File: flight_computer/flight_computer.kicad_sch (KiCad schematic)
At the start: 2 parts, among them U2 STM8S007C8T6

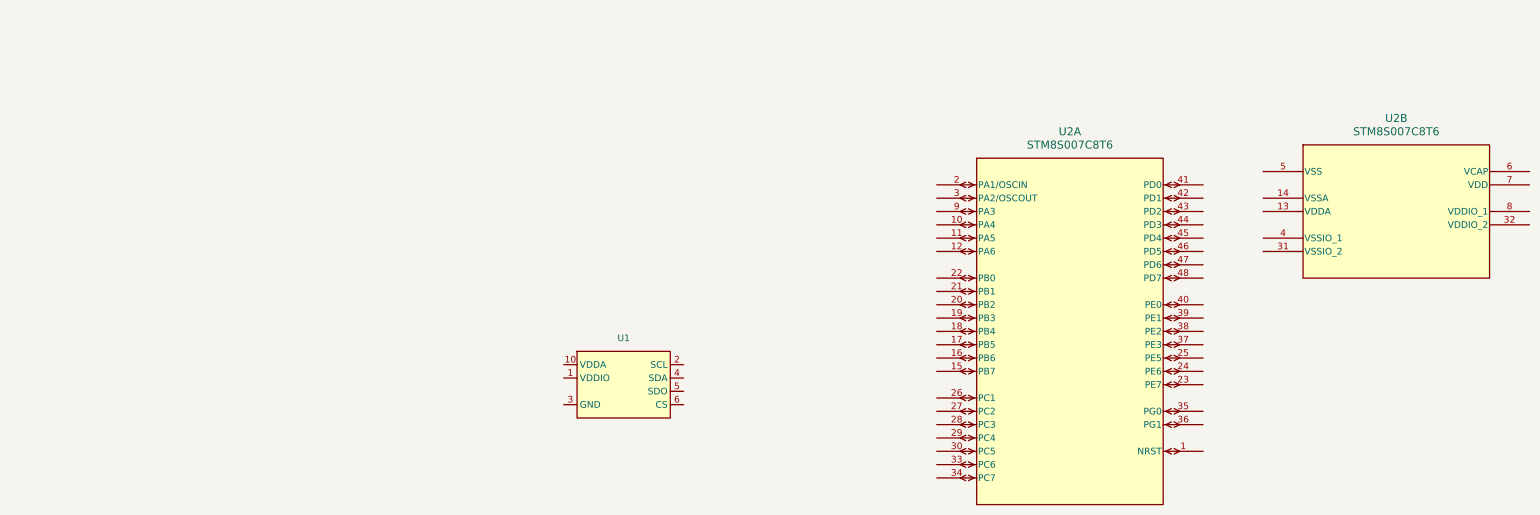
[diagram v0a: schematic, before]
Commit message: Finished power input design
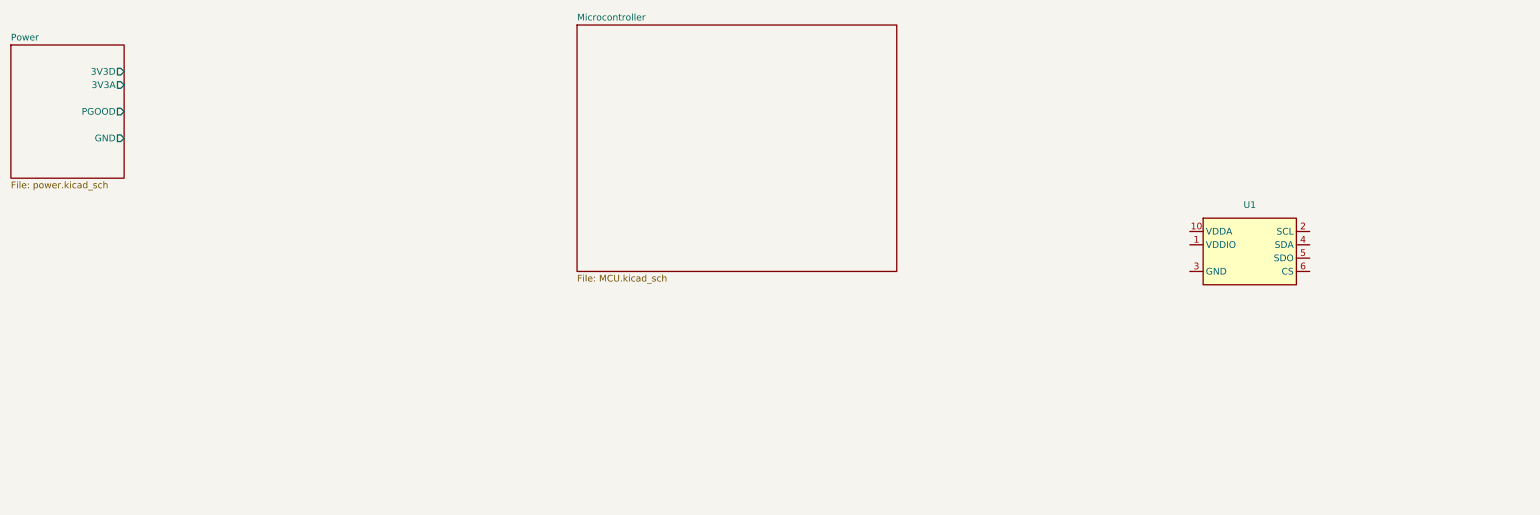
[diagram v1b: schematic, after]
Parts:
- removed U2: STM8S007C8T6, Package_QFP:LQFP-48_7x7mm_P0.5mm, symbol my_library:STM8S007C8T6
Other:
- added sheet Microcontroller (MCU.kicad_sch)
- added sheet Power (power.kicad_sch)
- moved on the sheet: U1
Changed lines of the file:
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@@
 (kicad_sch (version 20230121) (generator eeschema)
   (paper "A3")
-  (symbol (lib_id "my_library:STM8S007C8T6") (at 273.05 113.03 0) (unit 1)
+  (symbol (lib_id "my_library:SPL07-003") (at 307.34 97.79 0) (unit 1)
     (in_bom yes) (on_board yes) (dnp no) (fields_autoplaced)
-    (property "Reference" "U2" (at 273.05 74.93 0)
-      (effects (font (size 1.524 1.524)))
-    )
-    (property "Value" "STM8S007C8T6" (at 273.05 77.47 0)
-      (effects (font (size 1.524 1.524)))
-    )
-    (property "Footprint" "Package_QFP:LQFP-48_7x7mm_P0.5mm" (at 247.65 85.09 0)
-      (effects (font (size 1.27 1.27) italic) hide)
-    )
-    (property "Datasheet" "https://www.st.com/content/ccc/resource/technical/document/datasheet/03/af/ba/15/7c/fe/4c/91/DM00037365.pdf/files/DM00037365.pdf/jcr:content/translations/en.DM00037365.pdf" (at 247.65 85.09 0)
-      (effects (font (size 1.27 1.27) italic) hide)
-    )
-    (pin "1")
-    (pin "10")
-    (pin "11")
-    (pin "12")
-    (pin "15")
-    (pin "16")
-    (pin "17")
-    (pin "18")
-    (pin "19")
-    (pin "2")
-    (pin "20")
-    (pin "21")
-    (pin "22")
-    (pin "23")
-    (pin "24")
-    (pin "25")
-    (pin "26")
-    (pin "27")
-    (pin "28")
-    (pin "29")
-    (pin "3")
-    (pin "30")
-    (pin "33")
-    (pin "34")
-    (pin "35")
-    (pin "36")
-    (pin "37")
-    (pin "38")
-    (pin "39")
-    (pin "40")
-    (pin "41")
-    (pin "42")
-    (pin "43")
-    (pin "44")
-    (pin "45")
-    (pin "46")
-    (pin "47")
-    (pin "48")
-    (pin "9")
-    (pin "13")
-    (pin "14")
-    (pin "31")
-    (pin "32")
-    (pin "4")
-    (pin "5")
-    (pin "6")
-    (pin "7")
-    (pin "8")
-    (instances
-      (project "flight_computer"
-        (path "/89a81c02-14e9-456f-a334-ff69a24bd093"
-          (reference "U2") (unit 1)
-        )
-      )
-    )
-  )
-  (symbol (lib_id "my_library:STM8S007C8T6") (at 335.28 90.17 0) (unit 2)
-    (in_bom yes) (on_board yes) (dnp no) (fields_autoplaced)
-    (property "Reference" "U2" (at 335.28 72.39 0)
-      (effects (font (size 1.524 1.524)))
-    )
-    (property "Value" "STM8S007C8T6" (at 335.28 74.93 0)
-      (effects (font (size 1.524 1.524)))
-    )
-    (property "Footprint" "Package_QFP:LQFP-48_7x7mm_P0.5mm" (at 309.88 62.23 0)
-      (effects (font (size 1.27 1.27) italic) hide)
-    )
-    (property "Datasheet" "https://www.st.com/content/ccc/resource/technical/document/datasheet/03/af/ba/15/7c/fe/4c/91/DM00037365.pdf/files/DM00037365.pdf/jcr:content/translations/en.DM00037365.pdf" (at 309.88 62.23 0)
-      (effects (font (size 1.27 1.27) italic) hide)
-    )
-    (pin "1")
-    (pin "10")
-    (pin "11")
-    (pin "12")
-    (pin "15")
-    (pin "16")
-    (pin "17")
-    (pin "18")
-    (pin "19")
-    (pin "2")
-    (pin "20")
-    (pin "21")
-    (pin "22")
-    (pin "23")
-    (pin "24")
-    (pin "25")
-    (pin "26")
-    (pin "27")
-    (pin "28")
-    (pin "29")
-    (pin "3")
-    (pin "30")
-    (pin "33")
-    (pin "34")
-    (pin "35")
-    (pin "36")
-    (pin "37")
-    (pin "38")
-    (pin "39")
-    (pin "40")
-    (pin "41")
-    (pin "42")
-    (pin "43")
-    (pin "44")
-    (pin "45")
-    (pin "46")
-    (pin "47")
-    (pin "48")
-    (pin "9")
-    (pin "13")
-    (pin "14")
-    (pin "31")
-    (pin "32")
-    (pin "4")
-    (pin "5")
-    (pin "6")
-    (pin "7")
-    (pin "8")
-    (instances
-      (project "flight_computer"
-        (path "/89a81c02-14e9-456f-a334-ff69a24bd093"
-          (reference "U2") (unit 2)
-        )
-      )
-    )
-  )
-  (symbol (lib_id "my_library:SPL07-003") (at 187.96 123.19 0) (unit 1)
-    (in_bom yes) (on_board yes) (dnp no) (fields_autoplaced)
-    (property "Reference" "U1" (at 187.96 114.3 0)
+    (property "Reference" "U1" (at 307.34 88.9 0)
       (effects (font (size 1.27 1.27)))
     )
-    (property "Value" "~" (at 187.96 127 0)
+    (property "Value" "~" (at 307.34 101.6 0)
       (effects (font (size 1.27 1.27)))
     )
-    (property "Footprint" "Package_LGA:ST_HLGA-10_2x2mm_P0.5mm_LayoutBorder3x2y" (at 187.96 127 0)
+    (property "Footprint" "Package_LGA:ST_HLGA-10_2x2mm_P0.5mm_LayoutBorder3x2y" (at 307.34 101.6 0)
       (effects (font (size 1.27 1.27)) hide)
     )
-    (property "Datasheet" "https://mm.digikey.com/Volume0/opasdata/d220001/medias/docus/4843/SPL07-003.pdf" (at 187.96 127 0)
+    (property "Datasheet" "https://mm.digikey.com/Volume0/opasdata/d220001/medias/docus/4843/SPL07-003.pdf" (at 307.34 101.6 0)
       (effects (font (size 1.27 1.27)) hide)
     )
-    (property "Manufacturer PN" "" (at 187.96 123.19 0)
+    (property "Manufacturer PN" "" (at 307.34 97.79 0)
       (effects (font (size 1.27 1.27)) hide)
     )
-    (property "Supplier PN" "" (at 187.96 123.19 0)
+    (property "Supplier PN" "" (at 307.34 97.79 0)
       (effects (font (size 1.27 1.27)) hide)
     )
-    (property "Supplier" "" (at 187.96 123.19 0)
+    (property "Supplier" "" (at 307.34 97.79 0)
       (effects (font (size 1.27 1.27)) hide)
     )
@@
       )
     )
+  )
+  (sheet (at 179.07 54.61) (size 60.96 46.99) (fields_autoplaced)
+    (stroke (width 0.1524) (type solid))
+    (fill (color 0 0 0 0.0000))
+    (property "Sheetname" "Microcontroller" (at 179.07 53.8984 0)
+      (effects (font (size 1.27 1.27)) (justify left bottom))
+    )
+    (property "Sheetfile" "MCU.kicad_sch" (at 179.07 102.1846 0)
+      (effects (font (size 1.27 1.27)) (justify left top))
+    )
+    (instances
+      (project "flight_computer"
+        (path "/89a81c02-14e9-456f-a334-ff69a24bd093" (page "2"))
+      )
+    )
+  )
+  (sheet (at 71.12 58.42) (size 21.59 25.4) (fields_autoplaced)
+    (stroke (width 0.1524) (type solid))
+    (fill (color 0 0 0 0.0000))
+    (property "Sheetname" "Power" (at 71.12 57.7084 0)
+      (effects (font (size 1.27 1.27)) (justify left bottom))
+    )
+    (property "Sheetfile" "power.kicad_sch" (at 71.12 84.4046 0)
+      (effects (font (size 1.27 1.27)) (justify left top))
+    )
+    (pin "PGOOD" output (at 92.71 71.12 0)
+      (effects (font (size 1.27 1.27)) (justify right))
+    )
+    (pin "GND" output (at 92.71 76.2 0)
+      (effects (font (size 1.27 1.27)) (justify right))
+    )
+    (pin "3V3D" output (at 92.71 63.5 0)
+      (effects (font (size 1.27 1.27)) (justify right))
+    )
+    (pin "3V3A" output (at 92.71 66.04 0)
+      (effects (font (size 1.27 1.27)) (justify right))
+    )
+    (instances
+      (project "flight_computer"
+        (path "/89a81c02-14e9-456f-a334-ff69a24bd093" (page "3"))
+      )
+    )

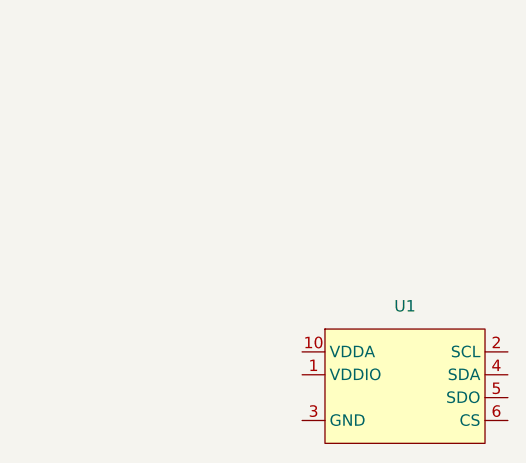
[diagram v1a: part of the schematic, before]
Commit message: Buzzer, LEDs, added actual components for current sensing and others I had missed
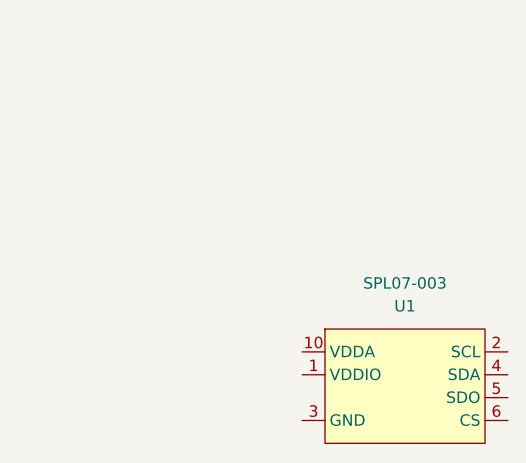
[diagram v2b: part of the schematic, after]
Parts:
- U1: value ~ -> SPL07-003; Manufacturer PN (none) -> SPL07-003; Supplier (none) -> Digikey; Supplier PN (none) -> 4719-SPL07-003CT-ND
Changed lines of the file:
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@@
   (paper "A3")
   (symbol (lib_id "my_library:SPL07-003") (at 307.34 97.79 0) (unit 1)
-    (in_bom yes) (on_board yes) (dnp no) (fields_autoplaced)
+    (in_bom yes) (on_board yes) (dnp no)
     (property "Reference" "U1" (at 307.34 88.9 0)
       (effects (font (size 1.27 1.27)))
     )
-    (property "Value" "~" (at 307.34 101.6 0)
+    (property "Value" "SPL07-003" (at 307.34 86.36 0)
       (effects (font (size 1.27 1.27)))
     )
@@
       (effects (font (size 1.27 1.27)) hide)
     )
-    (property "Manufacturer PN" "" (at 307.34 97.79 0)
+    (property "Manufacturer PN" "SPL07-003" (at 307.34 97.79 0)
       (effects (font (size 1.27 1.27)) hide)
     )
-    (property "Supplier PN" "" (at 307.34 97.79 0)
+    (property "Supplier PN" "4719-SPL07-003CT-ND" (at 307.34 97.79 0)
       (effects (font (size 1.27 1.27)) hide)
     )
-    (property "Supplier" "" (at 307.34 97.79 0)
+    (property "Supplier" "Digikey" (at 307.34 97.79 0)
       (effects (font (size 1.27 1.27)) hide)
     )

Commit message: PRessure sensor circuit
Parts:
- removed U1: SPL07-003, Package_LGA:ST_HLGA-10_2x2mm_P0.5mm_LayoutBorder3x2y, symbol my_library:SPL07-003
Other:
- added sheet Sensors (sensors.kicad_sch)
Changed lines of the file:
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@@
 (kicad_sch (version 20230121) (generator eeschema)
   (paper "A3")
-  (symbol (lib_id "my_library:SPL07-003") (at 307.34 97.79 0) (unit 1)
-    (in_bom yes) (on_board yes) (dnp no)
-    (property "Reference" "U1" (at 307.34 88.9 0)
-      (effects (font (size 1.27 1.27)))
-    )
-    (property "Value" "SPL07-003" (at 307.34 86.36 0)
-      (effects (font (size 1.27 1.27)))
-    )
-    (property "Footprint" "Package_LGA:ST_HLGA-10_2x2mm_P0.5mm_LayoutBorder3x2y" (at 307.34 101.6 0)
-      (effects (font (size 1.27 1.27)) hide)
-    )
-    (property "Datasheet" "https://mm.digikey.com/Volume0/opasdata/d220001/medias/docus/4843/SPL07-003.pdf" (at 307.34 101.6 0)
-      (effects (font (size 1.27 1.27)) hide)
-    )
-    (property "Manufacturer PN" "SPL07-003" (at 307.34 97.79 0)
-      (effects (font (size 1.27 1.27)) hide)
-    )
-    (property "Supplier PN" "4719-SPL07-003CT-ND" (at 307.34 97.79 0)
-      (effects (font (size 1.27 1.27)) hide)
-    )
-    (property "Supplier" "Digikey" (at 307.34 97.79 0)
-      (effects (font (size 1.27 1.27)) hide)
-    )
-    (pin "1")
-    (pin "10")
-    (pin "2")
-    (pin "3")
-    (pin "4")
-    (pin "5")
-    (pin "6")
-    (pin "7")
-    (pin "8")
-    (pin "9")
-    (instances
-      (project "flight_computer"
-        (path "/89a81c02-14e9-456f-a334-ff69a24bd093"
-          (reference "U1") (unit 1)
-        )
-      )
-    )
-  )
   (sheet (at 179.07 54.61) (size 60.96 46.99) (fields_autoplaced)
     (stroke (width 0.1524) (type solid))
@@
       )
     )
+  )
+  (sheet (at 160.02 157.48) (size 50.8 44.45) (fields_autoplaced)
+    (stroke (width 0.1524) (type solid))
+    (fill (color 0 0 0 0.0000))
+    (property "Sheetname" "Sensors" (at 160.02 156.7684 0)
+      (effects (font (size 1.27 1.27)) (justify left bottom))
+    )
+    (property "Sheetfile" "sensors.kicad_sch" (at 160.02 202.5146 0)
+      (effects (font (size 1.27 1.27)) (justify left top))
+    )
+    (instances
+      (project "flight_computer"
+        (path "/89a81c02-14e9-456f-a334-ff69a24bd093" (page "4"))
+      )
+    )
